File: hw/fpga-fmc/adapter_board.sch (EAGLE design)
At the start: 176 parts, among them IC1 M24C02, J1 5569262-1, J2 ASP-134488-01, U1 ADM3066E, U10 ADM3066E, U11 ADM3066E, U12 ADM3066E, U13 ADM3066E, U14 ADM3066E, U15 ADM3066E, U16 ADM3066E, U17 TCA9548A, U18 TXS0102, U19 TXS0102, U2 ADM3066E, U20 TXS0102, U21 TXS0102, U3 ADM3066E, U4 ADM3066E, U40 IRLML2502, U5 ADM3066E, U6 ADM3066E, U7 ADM3066E, U8 ADM3066E, U9 ADM3066E

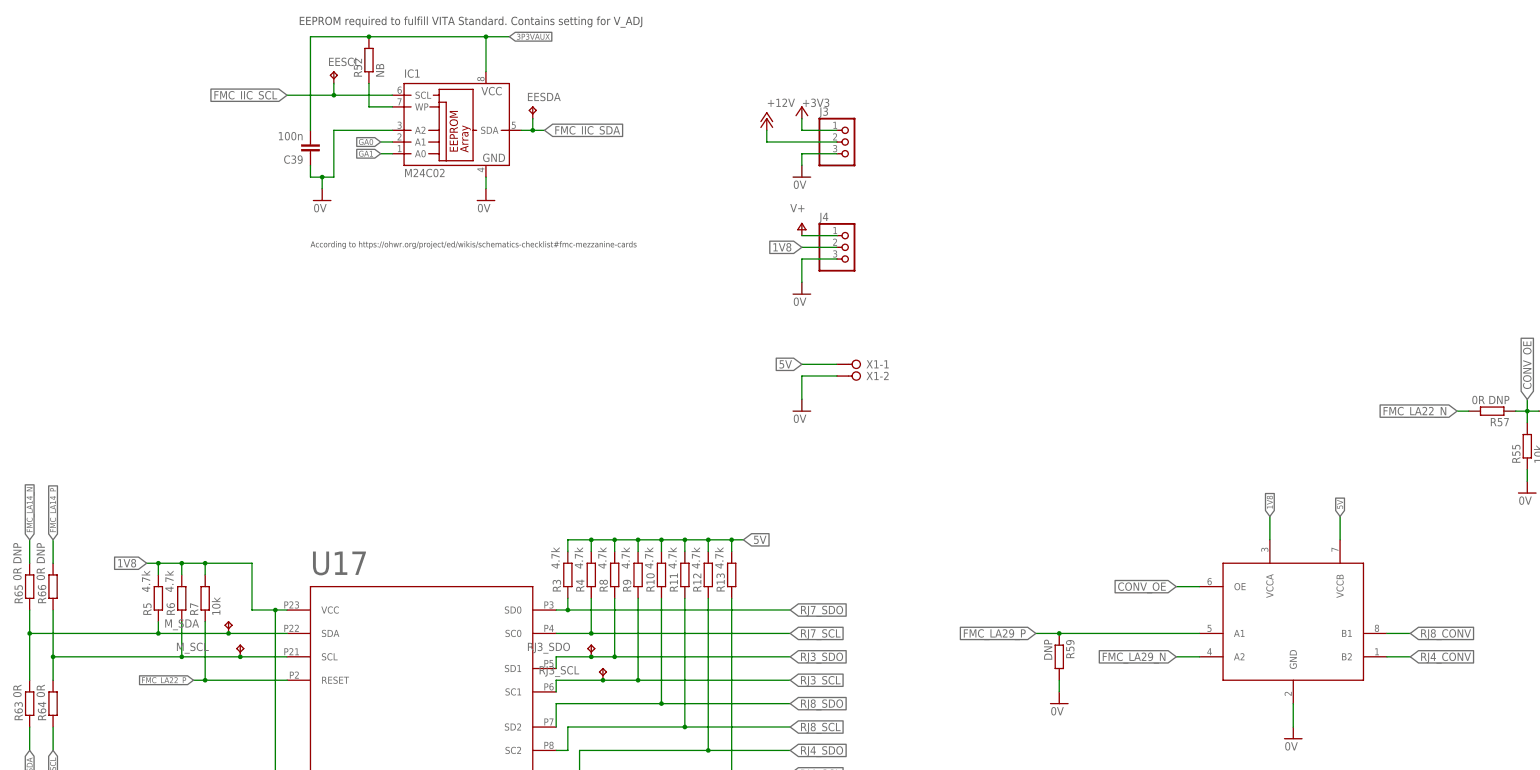
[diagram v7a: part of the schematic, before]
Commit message: hw/fpga-fmc: rewire pin header and screw terminal.
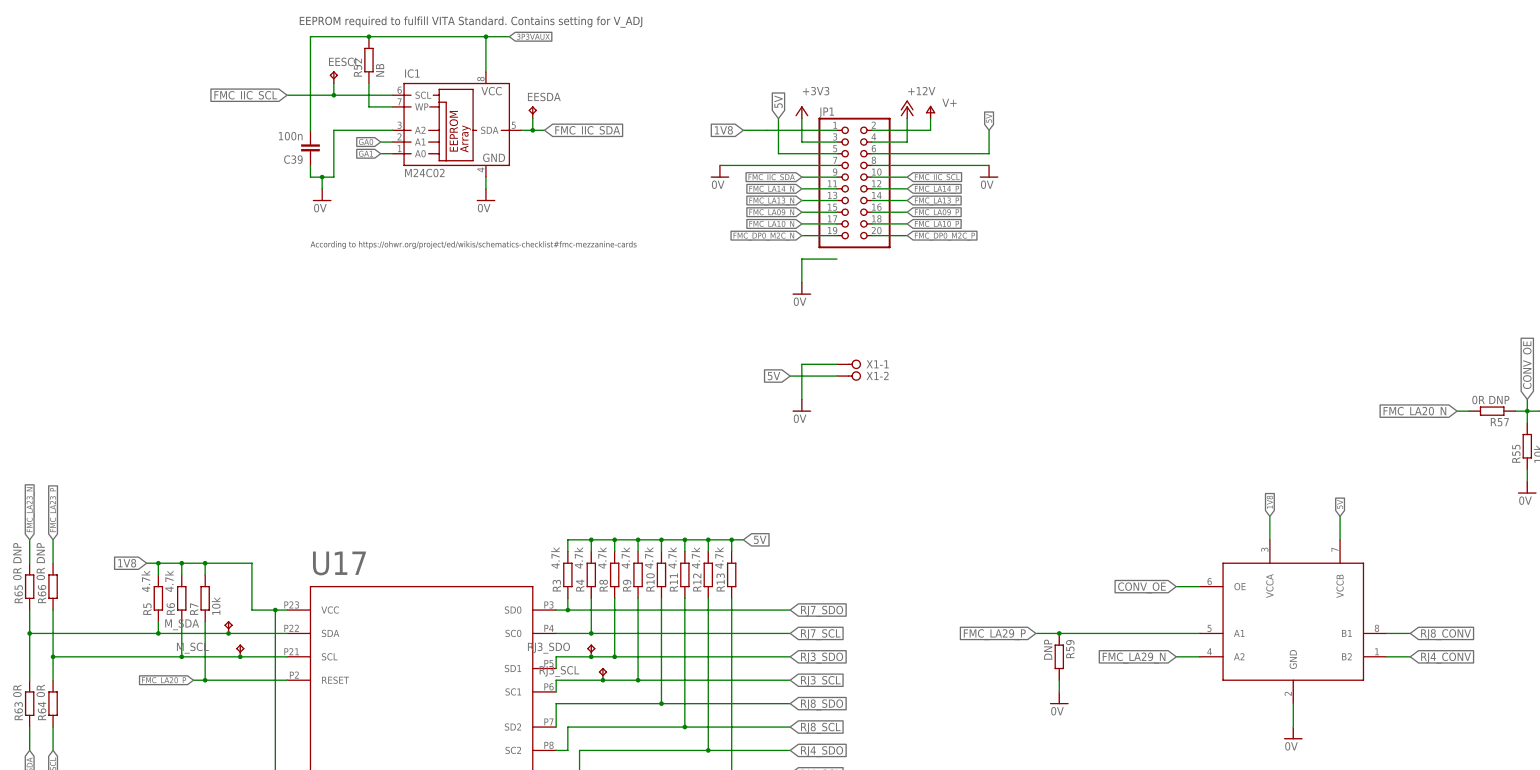
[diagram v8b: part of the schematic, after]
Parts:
- removed J3, J4: (no value), pinhead:PINHD-1X3
- added JP1: (no value), pinhead:PINHD-2X10
- C1, C10, C11, C12, C13, C14, C15, C16, C17, C18, C19, C2, C20, C21, C22, C23, C24, C25, C26, C27, C28, C29, C30, C31, C32, C33, C34, C35, C36, C37, C39, C5, C6, C7, C8, C9: device rcl:C-EUC0805 -> rcl:C-EUC0603
- R1, R2, R22, R23, R24, R25, R26, R27, R28, R29, R30, R31, R32, R33, R34, R35, R36, R37, R38, R39, R40, R41, R42, R43, R44, R45, R46, R47, R48, R49, R5, R50, R51, R52, R55, R57, R58, R6, R7: device rcl:R-EU_R0805 -> rcl:R-EU_R0603
- R60, R61: device resistor:R-EU_R0805 -> resistor:R-EU_R0603
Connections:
- net +12V: now also JP1.4; no longer J3.2
- net +3V3: now also JP1.3; no longer J3.1
- net 0V: now also JP1.7, JP1.8, X1-1.KL; no longer J3.3, J4.3, X1-2.KL
- net 1V8: now also JP1.1; no longer J4.2
- net 5V: now also JP1.5, JP1.6, X1-2.KL; no longer X1-1.KL
- net FMC_DP0_M2C_N: now also JP1.19
- net FMC_DP0_M2C_P: now also JP1.20
- net FMC_IIC_SCL: now also JP1.10
- net FMC_IIC_SDA: now also JP1.9
- net FMC_LA09_N: now also JP1.15
- net FMC_LA09_P: now also JP1.16
- net FMC_LA10_N: now also JP1.17
- net FMC_LA10_P: now also JP1.18
- net FMC_LA13_N: now also JP1.13
- net FMC_LA13_P: now also JP1.14
- net FMC_LA14_N: now also JP1.11; no longer R65.2
- net FMC_LA14_P: now also JP1.12; no longer R66.2
- net FMC_LA20_N: now also R57.2
- net FMC_LA20_P: now also R7.1, U17.RESET
- net FMC_LA22_N: no longer R57.2
- net FMC_LA22_P: no longer R7.1, U17.RESET
- net FMC_LA23_N: now also R65.2
- net FMC_LA23_P: now also R66.2
- net V+: now also JP1.2; no longer J4.1
